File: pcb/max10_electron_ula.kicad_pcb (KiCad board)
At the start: 4 copper layers, 55 x 89 mm, 86 parts

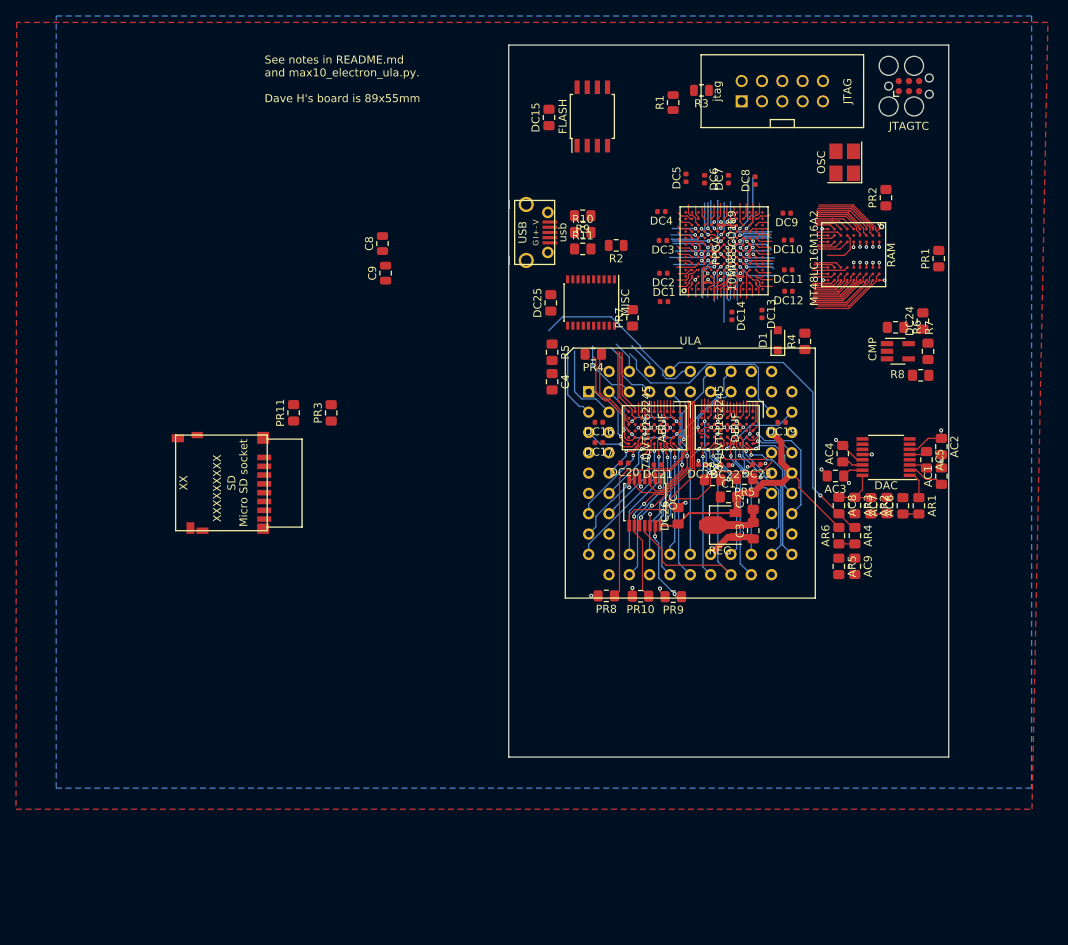
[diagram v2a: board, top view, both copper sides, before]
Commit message: Provisional FPGA pinout -- still need to check high/low speed pins, but it'll be similar to this
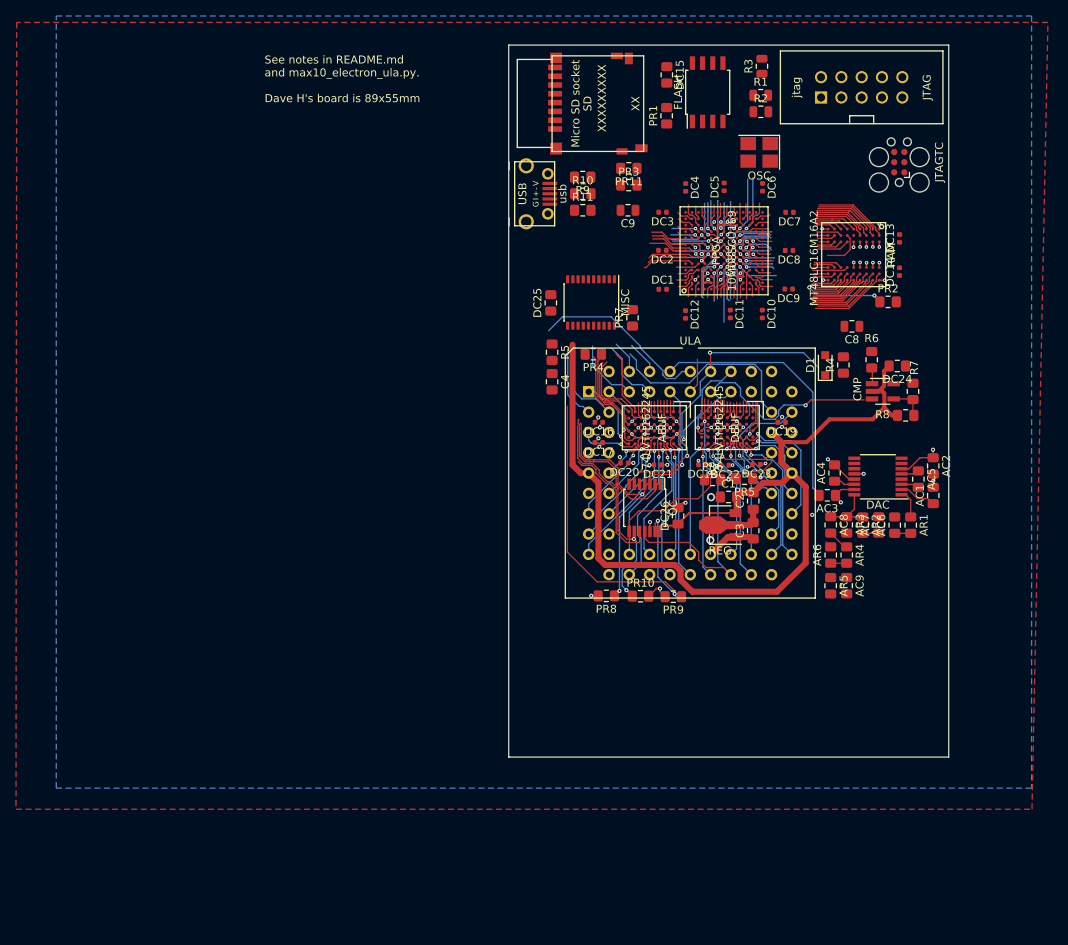
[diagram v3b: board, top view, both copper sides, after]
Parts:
- moved SD 75.3 mm to (164.1, 24.8), turned to 270 degrees
- moved C8 59.6 mm to (190.1, 52.6), turned to 180 degrees
- moved PR11 51.9 mm to (162.2, 32.9), turned to 180 degrees
- moved PR3 46.8 mm to (162.2, 34.9), turned to 0 degrees
- moved PR1 38.4 mm to (167.0, 26.3)
- moved C9 31.3 mm to (162.1, 38.1), turned to 180 degrees
- moved R2 24.6 mm to (178.7, 25.8), turned to 0 degrees
- moved DC14 21.7 mm to (196.1, 45.8), turned to 90 degrees
- moved DC13 19.6 mm to (196.1, 41.6), turned to 90 degrees
- moved DC15 15.7 mm to (167.0, 21.2), turned to 270 degrees
- moved FLASH 14.7 mm to (172.1, 23.3)
- moved DC12 13.2 mm to (169.3, 51.1), turned to 270 degrees
- moved PR2 13.0 mm to (194.6, 49.5), turned to 0 degrees
- moved R1 11.0 mm to (178.7, 23.7), turned to 0 degrees
- moved OSC 10.8 mm to (178.5, 30.9), turned to 180 degrees
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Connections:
- net io_b6_R18n_E12 renamed fpga_dummy3
- net io_b6_R33n_D11 renamed fpga_dummy1
- net special_b6_CLK3n_R16n_E13 renamed fpga_dummy2
- net special_b6_DPCLK2_R26n_F10 renamed fpga_dummy0
- FPGA pad A10: io_b8_T17p_A10 -> A_buf_DIR
- FPGA pad A11: io_b8_T17n_A11 -> casMO
- FPGA pad A12: io_b6_R30n_A12 -> blue
- FPGA pad A2: io_b8_T26p_A2 -> ROM_n
- FPGA pad A3: io_b8_T21n_A3 -> addr15
- FPGA pad A4: io_b8_T21p_A4 -> addr10
- FPGA pad A5: TODO_unknown_b8_A5 -> addr3
- FPGA pad A6: io_b8_T19n_A6 -> addr4
- FPGA pad A7: io_b8_T19p_A7 -> addr7
- FPGA pad A8: io_b8_T15p_A8 -> addr12
- FPGA pad A9: io_b8_T15n_A9 -> addr1
- FPGA pad B1: io_b1A_L5p_B1 -> kbd1
- FPGA pad B10: io_b8_T16p_B10 -> misc_buf_nOE
- FPGA pad B11: io_b6_R28n_B11 -> csync
- FPGA pad B12: io_b6_R28p_B12 -> green
- FPGA pad B13: io_b6_R30p_B13 -> HS_n
- FPGA pad B2: io_b8_T26n_B2 -> input_buf_nOE
- FPGA pad B3: io_b8_T23p_B3 -> kbd0
- FPGA pad B4: io_b8_T23n_B4 -> addr9
- FPGA pad B5: io_b8_T20n_B5 -> addr11
- FPGA pad B6: io_b8_T20p_B6 -> addr6
- FPGA pad B7: special_VREFB8N0_nodiff_B7 -> addr2
- FPGA pad C1: io_b1A_L5n_C1 -> IRQ_n_in
- FPGA pad C10: io_b8_T14p_C10 -> casOut
- FPGA pad C11: io_b6_R29n_C11 -> red
- FPGA pad C12: io_b6_R29p_C12 -> clk_out
- FPGA pad C13: TODO_unknown_b6_C13 -> RST_n_out
- FPGA pad C2: io_b1A_L1p_C2 -> NMI_n_in
- FPGA pad C9: io_b8_T14n_C9 -> A_buf_nOE
- FPGA pad D1: io_b1A_L1n_D1 -> kbd3
- FPGA pad D12: io_b6_R33p_D12 -> caps
- FPGA pad D13: special_VREFB6N0_nodiff_D13 -> RnW_nOE
- FPGA pad D6: fpga_CRC_ERROR -> GND
- FPGA pad D7: fpga_CONFIG_SEL -> GND
- FPGA pad D9: io_b6_R31n_D9 -> addr8
- FPGA pad E1: io_b1A_L7p_E1 -> clk_in
- FPGA pad E10: io_b6_R31p_E10 -> IRQ_n_out
- FPGA pad E3: io_b1A_L3n_E3 -> RnW_in
- FPGA pad E4: io_b1A_L3p_E4 -> kbd2
- FPGA pad E5: fpga_JTAGEN -> (no net)
- FPGA pad E6: io_b8_T22p_E6 -> addr5
- FPGA pad E7: fpga_nCONFIG -> 3V3
- FPGA pad E8: io_b8_T18n_E8 -> addr14
- FPGA pad E9: io_b6_R27n_E9 -> addr0
- FPGA pad F1: io_b1A_L7n_F1 -> data3
- FPGA pad F12: io_b6_R18p_F12 -> USB_PU
- FPGA pad F13: special_b6_CLK3p_R16p_F13 -> USB_M
- FPGA pad F4: io_b1B_L14n_F4 -> data0
- FPGA pad F8: io_b6_R27p_F8 -> addr13
- FPGA pad F9: special_b6_DPCLK3_R26p_F9 -> RnW_out
- FPGA pad G10: special_b6_CLK2n_R14n_G10 -> sd_CMD_MOSI
- FPGA pad G12: io_b5_R11n_G12 -> sd_DAT0_MISO
- FPGA pad G13: io_b5_R11p_G13 -> sd_CLK_SCK
- FPGA pad G4: io_b1B_L14p_G4 -> data7
- FPGA pad G5: special_b2_CLK0n_L18n_G5 -> data6
- FPGA pad G9: special_b6_CLK2p_R14p_G9 -> USB_P
- FPGA pad H1: special_VREFB1N0_nodiff_H1 -> D_buf_nOE
- FPGA pad H10: io_b5_R8n_H10 -> sd_DAT2
- FPGA pad H13: io_b5_R9n_H13 -> sd_DAT1
- FPGA pad H2: io_b1B_L16n_H2 -> data1
- FPGA pad H3: io_b1B_L16p_H3 -> data2
- FPGA pad H4: special_b2_CLK1p_L20p_H4 -> data5
- FPGA pad H5: special_b2_CLK1n_L20n_H5 -> casIn
- FPGA pad H6: special_b2_CLK0p_L18p_H6 -> data4
- FPGA pad H8: io_b5_R10n_H8 -> sdram_A4
- FPGA pad H9: io_b5_R10p_H9 -> sdram_UDQM
- FPGA pad J1: io_b2_L19n_J1 -> RST_n_in
- FPGA pad J10: io_b5_R1n_J10 -> flash_IO2
- FPGA pad J12: io_b5_R7n_J12 -> sd_DAT3_nCS
- FPGA pad J13: io_b5_R9p_J13 -> flash_nCE
- FPGA pad J2: io_b2_L19p_J2 -> D_buf_DIR
- FPGA pad J5: io_b3_B3p_J5 -> sdram_DQ6
- FPGA pad J6: io_b3_B7n_J6 -> sdram_nCS
- FPGA pad J7: io_b3_B9n_J7 -> sdram_A2
- FPGA pad J8: io_b3_B14n_J8 -> sdram_A7
- FPGA pad J9: io_b5_R8p_J9 -> sdram_A8
- FPGA pad K1: io_b2_L28n_K1 -> dac_mclk
- FPGA pad K10: io_b5_R1p_K10 -> clk_osc
- FPGA pad K11: io_b5_R2p_K11 -> flash_SCK
- FPGA pad K12: io_b5_R7p_K12 -> flash_IO1
- FPGA pad K13: special_VREFB5N0_nodiff_K13 -> flash_IO0
- FPGA pad K2: io_b2_L28p_K2 -> dac_bclk
- FPGA pad K5: io_b3_B3n_K5 -> sdram_nWE
- FPGA pad K6: io_b3_B7p_K6 -> sdram_A1
- FPGA pad K7: io_b3_B9p_K7 -> sdram_CLK
- FPGA pad K8: io_b3_B14p_K8 -> sdram_BA0
- FPGA pad L1: special_VREFB2N0_nodiff_L1 -> dac_dacdat
- FPGA pad L10: io_b3_B16p_L10 -> sdram_DQ8
- FPGA pad L11: io_b3_B12p_L11 -> sdram_DQ13
- FPGA pad L12: io_b5_R2n_L12 -> flash_IO3
- FPGA pad L13: TODO_unknown_b5_L13 -> sdram_DQ15
- FPGA pad L2: TODO_unknown_b2_L2 -> dac_lrclk
- FPGA pad L3: special_b2_PLL_L_CLKOUTp_L27p_L3 -> sdram_DQ2
- FPGA pad L4: io_b3_B1p_L4 -> dac_nmute
- FPGA pad L5: io_b3_B1n_L5 -> sdram_A10
- FPGA pad M1: io_b2_L21n_M1 -> sdram_DQ0
- FPGA pad M10: io_b3_B16n_M10 -> sdram_A11
- FPGA pad M11: io_b3_B12n_M11 -> sdram_DQ10
- FPGA pad M12: io_b3_B10p_M12 -> sdram_DQ12
- FPGA pad M13: io_b3_B10n_M13 -> sdram_DQ14
- FPGA pad M2: io_b2_L21p_M2 -> sdram_DQ1
- FPGA pad M3: special_b2_PLL_L_CLKOUTn_L27n_M3 -> sdram_DQ4
- FPGA pad M4: io_b3_B2n_M4 -> sdram_DQ7
- FPGA pad M5: io_b3_B2p_M5 -> sdram_nRAS
- FPGA pad M7: io_b3_B5p_M7 -> sdram_A3
- FPGA pad M8: io_b3_B8n_M8 -> sdram_CKE
- FPGA pad M9: io_b3_B8p_M9 -> sdram_A6
- FPGA pad N10: io_b3_B11n_N10 -> sdram_A12
- FPGA pad N11: special_VREFB3N0_nodiff_N11 -> sdram_DQ9
- FPGA pad N12: TODO_unknown_b3_N12 -> sdram_DQ11
- FPGA pad N2: special_b2_DPCLK0_L22n_N2 -> sdram_DQ3
- FPGA pad N3: special_b2_DPCLK1_L22p_N3 -> sdram_DQ5
- FPGA pad N4: io_b3_B4n_N4 -> sdram_LDQM
- FPGA pad N5: io_b3_B4p_N5 -> sdram_BA1
- FPGA pad N6: io_b3_B5n_N6 -> sdram_nCAS
- FPGA pad N7: io_b3_B6n_N7 -> sdram_A0
- FPGA pad N8: io_b3_B6p_N8 -> sdram_A9
- FPGA pad N9: io_b3_B11p_N9 -> sdram_A5
- SD pad 1: (no net) -> sd_DAT2
- ULA pad 9: (no net) -> 5V
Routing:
- net 5V: track 35.6 -> 122.3 mm
- net CAS_IN_5V: track 0.00 -> 23.5 mm, vias 0 -> 1
- net IRQ_n_out: track 29.6 -> 50.4 mm
- net sdram_nCS: track 3.95 -> 18.9 mm, vias 0 -> 3
- net nRESET_5V: track 23.0 -> 37.7 mm, vias 1 -> 2
- net caps: track 12.6 -> 20.4 mm
- net special_b2_CLK1p_L20p_H4: track 7.67 -> 0.00 mm, vias 1 -> 0
- net data5: track 1.31 -> 8.98 mm, vias 0 -> 1
- net io_b5_R1p_K10: track 7.24 -> 0.00 mm, vias 1 -> 0
- net clk_osc: track 0.00 -> 7.24 mm, vias 0 -> 1
- net io_b5_R1n_J10: track 7.13 -> 0.00 mm, vias 1 -> 0
- net flash_IO2: track 0.00 -> 7.13 mm, vias 0 -> 1
- net casIn: track 0.00 -> 6.99 mm, vias 0 -> 1
- net addr11: track 2.33 -> 8.81 mm
- net sdram_UDQM: track 4.35 -> 10.6 mm, vias 0 -> 1
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
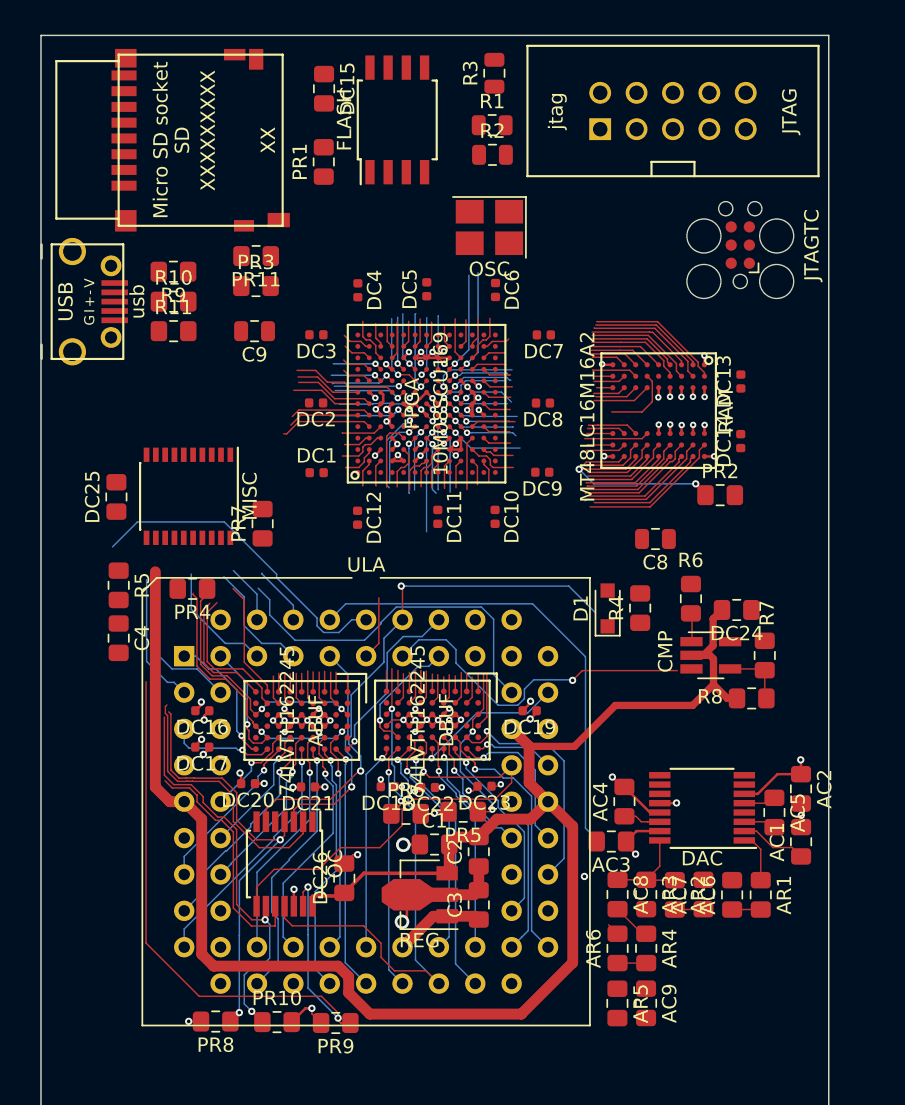
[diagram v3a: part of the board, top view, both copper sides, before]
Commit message: Wiring for ULA looking pretty good now -- doing top parts
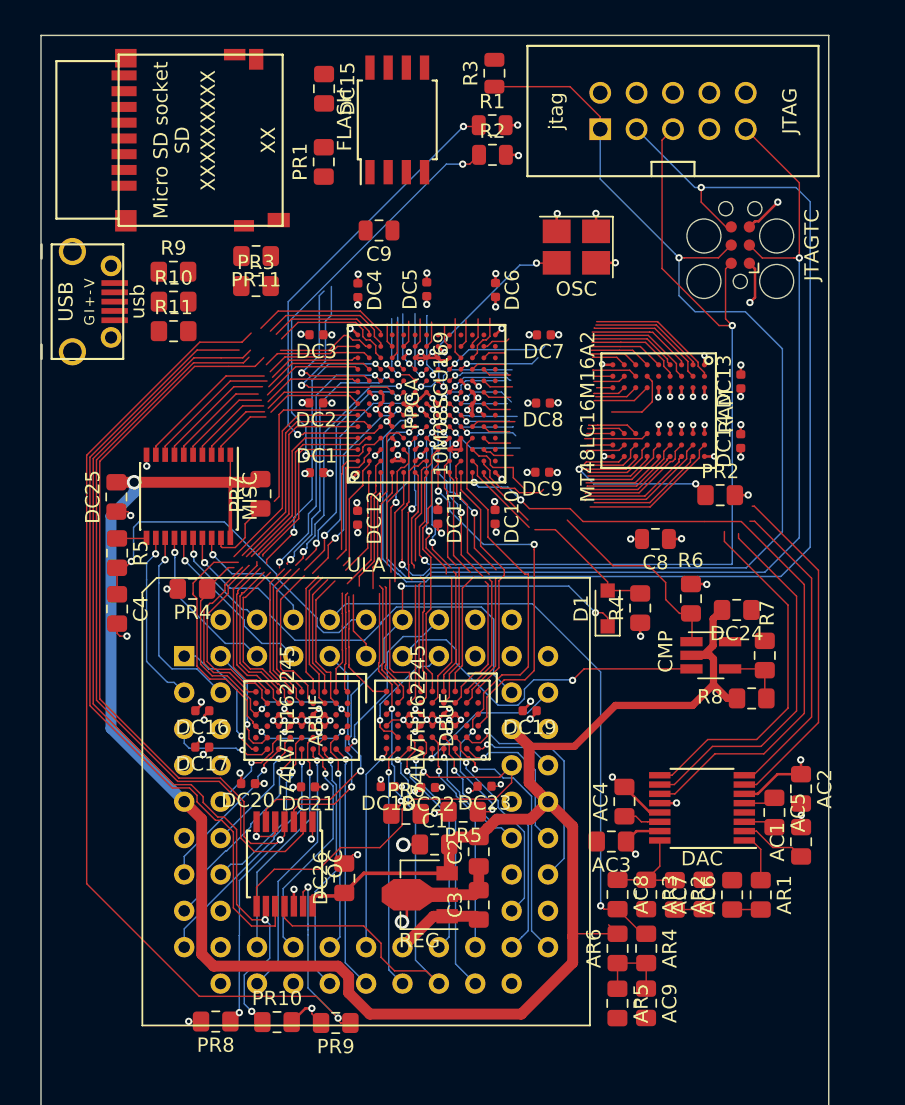
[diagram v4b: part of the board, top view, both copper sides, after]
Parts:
- moved C9 11.2 mm to (170.8, 31.1)
- moved OSC 6.22 mm to (184.6, 32.2)
- moved R5 2.25 mm to (152.5, 53.6)
- moved PR7 2.10 mm to (162.6, 49.4)
- moved C4 2.04 mm to (152.5, 57.5)
- turned R9 to 0 degrees
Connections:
- FPGA pad A10: A_buf_DIR -> csync
- FPGA pad A11: casMO -> green
- FPGA pad A12: blue -> clk_out
- FPGA pad A2: ROM_n -> addr11
- FPGA pad A3: addr15 -> addr14
- FPGA pad A4: addr10 -> addr8
- FPGA pad A5: addr3 -> addr1
- FPGA pad A6: addr4 -> A_buf_DIR
- FPGA pad A7: addr7 -> casMO
- FPGA pad A8: addr12 -> casOut
- FPGA pad A9: addr1 -> blue
- FPGA pad B1: kbd1 -> addr9
- FPGA pad B10: misc_buf_nOE -> HS_n
- FPGA pad B11: csync -> red
- FPGA pad B12: green -> RST_n_out
- FPGA pad B13: HS_n -> RnW_nOE
- FPGA pad B2: input_buf_nOE -> addr10
- FPGA pad B3: kbd0 -> addr3
- FPGA pad B4: addr9 -> addr0
- FPGA pad B5: addr11 -> A_buf_nOE
- FPGA pad B6: addr6 -> misc_buf_nOE
- FPGA pad B7: addr2 -> fpga_dummy3
- FPGA pad C1: IRQ_n_in -> kbd0
- FPGA pad C10: casOut -> addr12
- FPGA pad C11: red -> caps
- FPGA pad C12: clk_out -> RnW_out
- FPGA pad C13: RST_n_out -> IRQ_n_out
- FPGA pad C2: NMI_n_in -> addr15
- FPGA pad C9: A_buf_nOE -> addr2
- FPGA pad D1: kbd3 -> input_buf_nOE
- FPGA pad D11: fpga_dummy1 -> sd_CMD_MOSI
- FPGA pad D12: caps -> USB_M
- FPGA pad D13: RnW_nOE -> fpga_dummy1
- FPGA pad D9: addr8 -> addr7
- FPGA pad E1: clk_in -> IRQ_n_in
- FPGA pad E10: IRQ_n_out -> USB_PU
- FPGA pad E12: fpga_dummy3 -> sd_DAT1
- FPGA pad E13: fpga_dummy2 -> sd_DAT0_MISO
- FPGA pad E3: RnW_in -> kbd1
- FPGA pad E4: kbd2 -> ROM_n
- FPGA pad E8: addr14 -> addr6
- FPGA pad E9: addr0 -> addr13
- FPGA pad F1: data3 -> kbd3
- FPGA pad F10: fpga_dummy0 -> sd_CLK_SCK
- FPGA pad F12: USB_PU -> sd_DAT3_nCS
- FPGA pad F13: USB_M -> sd_DAT2
- FPGA pad F4: data0 -> NMI_n_in
- FPGA pad F8: addr13 -> addr4
- FPGA pad F9: RnW_out -> USB_P
- FPGA pad G10: sd_CMD_MOSI -> flash_SCK
- FPGA pad G12: sd_DAT0_MISO -> flash_IO0
- FPGA pad G13: sd_CLK_SCK -> flash_nCE
- FPGA pad G4: data7 -> data6
- FPGA pad G5: data6 -> kbd2
- FPGA pad G9: USB_P -> clk_osc
- FPGA pad H1: D_buf_nOE -> D_buf_DIR
- FPGA pad H10: sd_DAT2 -> flash_IO2
- FPGA pad H13: sd_DAT1 -> flash_IO1
- FPGA pad H2: data1 -> clk_in
- FPGA pad H3: data2 -> RnW_in
- FPGA pad H4: data5 -> data0
- FPGA pad H5: casIn -> data4
- FPGA pad H6: data4 -> data1
- FPGA pad H8: sdram_A4 -> sdram_BA0
- FPGA pad H9: sdram_UDQM -> sdram_A7
- FPGA pad J1: RST_n_in -> data2
- FPGA pad J10: flash_IO2 -> sdram_DQ12
- FPGA pad J12: sd_DAT3_nCS -> flash_IO3
- FPGA pad J13: flash_nCE -> sdram_DQ15
- FPGA pad J2: D_buf_DIR -> data3
- FPGA pad J5: sdram_DQ6 -> sdram_DQ1
- FPGA pad J6: sdram_nCS -> sdram_DQ6
- FPGA pad J7: sdram_A2 -> sdram_nRAS
- FPGA pad J8: sdram_A7 -> sdram_CLK
- FPGA pad J9: sdram_A8 -> sdram_A6
- FPGA pad K1: dac_mclk -> data7
- FPGA pad K10: clk_osc -> sdram_DQ10
- FPGA pad K11: flash_SCK -> sdram_DQ14
- FPGA pad K12: flash_IO1 -> sdram_DQ13
- FPGA pad K13: flash_IO0 -> fpga_dummy0
- FPGA pad K2: dac_bclk -> data5
- FPGA pad K5: sdram_nWE -> sdram_DQ4
- FPGA pad K6: sdram_A1 -> sdram_nWE
- FPGA pad K7: sdram_CLK -> sdram_A2
- FPGA pad K8: sdram_BA0 -> sdram_A1
- FPGA pad L1: dac_dacdat -> dac_nmute
- FPGA pad L10: sdram_DQ8 -> sdram_A5
- FPGA pad L11: sdram_DQ13 -> sdram_UDQM
- FPGA pad L12: flash_IO3 -> sdram_DQ11
- FPGA pad L13: sdram_DQ15 -> sdram_DQ9
- FPGA pad L2: dac_lrclk -> RST_n_in
- FPGA pad L3: sdram_DQ2 -> dac_mclk
- FPGA pad L4: dac_nmute -> D_buf_nOE
- FPGA pad L5: sdram_A10 -> sdram_LDQM
- FPGA pad M1: sdram_DQ0 -> casIn
- FPGA pad M10: sdram_A11 -> sdram_A9
- FPGA pad M11: sdram_DQ10 -> sdram_A11
- FPGA pad M12: sdram_DQ12 -> sdram_A12
- FPGA pad M13: sdram_DQ14 -> sdram_DQ8
- FPGA pad M2: sdram_DQ1 -> dac_bclk
- FPGA pad M3: sdram_DQ4 -> dac_lrclk
- FPGA pad M4: sdram_DQ7 -> sdram_DQ2
- FPGA pad M5: sdram_nRAS -> sdram_DQ5
- FPGA pad M7: sdram_A3 -> sdram_BA1
- FPGA pad M8: sdram_CKE -> sdram_nCAS
- FPGA pad M9: sdram_A6 -> sdram_A0
- FPGA pad N10: sdram_A12 -> sdram_A4
- FPGA pad N11: sdram_DQ9 -> fpga_dummy2
- FPGA pad N12: sdram_DQ11 -> sdram_A8
- FPGA pad N2: sdram_DQ3 -> dac_dacdat
- FPGA pad N3: sdram_DQ5 -> sdram_DQ0
- FPGA pad N4: sdram_LDQM -> sdram_DQ3
- FPGA pad N5: sdram_BA1 -> sdram_DQ7
- FPGA pad N6: sdram_nCAS -> sdram_nCS
- FPGA pad N7: sdram_A0 -> sdram_A10
- FPGA pad N8: sdram_A9 -> sdram_A3
- FPGA pad N9: sdram_A5 -> sdram_CKE
- MISC pad 12: nHS_5V -> red_5V
- MISC pad 13: red_5V -> green_5V
- MISC pad 14: green_5V -> nHS_5V
- MISC pad 15: blue_5V -> csync_5V
- MISC pad 16: csync_5V -> blue_5V
- MISC pad 17: CAS_MO_5V -> CAS_OUT_5V
- MISC pad 18: CAS_OUT_5V -> CAS_MO_5V
- MISC pad 2: casOut -> casMO
- MISC pad 3: casMO -> casOut
- MISC pad 4: csync -> blue
- MISC pad 5: blue -> csync
- MISC pad 6: green -> HS_n
- MISC pad 7: red -> green
- MISC pad 8: HS_n -> red
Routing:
- net fpga_TCK: track 2.84 -> 84.9 mm, vias 0 -> 2
- net fpga_TDO: track 6.12 -> 85.0 mm, vias 1 -> 2
- net fpga_TDI: track 5.06 -> 75.0 mm, vias 1 -> 2
- net fpga_TMS: track 0.00 -> 66.0 mm, vias 0 -> 2
- net dac_nmute: track 3.75 -> 48.2 mm, vias 0 -> 2
- net RnW_out: track 22.1 -> 64.4 mm, vias 1 -> 0
- net RnW_nOE: track 28.4 -> 70.2 mm
- net RST_n_out: track 30.4 -> 71.8 mm
- net caps: track 20.4 -> 61.0 mm
- net IRQ_n_out: track 50.4 -> 88.7 mm, vias 3 -> 2
- net dac_mclk: track 0.00 -> 31.2 mm
- net fpga_CONF_DONE: track 2.88 -> 34.0 mm, vias 0 -> 2
- net fpga_nSTATUS: track 3.40 -> 33.7 mm, vias 0 -> 2
- net dac_bclk: track 2.01 -> 30.7 mm
- net 5V: track 122.3 -> 149.1 mm, vias 0 -> 1
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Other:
- board text added: "<- d13 slow vref"
- board text added: "<- k13 slow vref"
- board text added: "<- n11 slow vref"
- board text added: "b7 slow vref ->"
- board text added: "h1 slow vref ->"
- board text added: "l1 slow vref ->"
